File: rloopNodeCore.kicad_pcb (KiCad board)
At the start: 2 copper layers, 47 parts, among them P1 PWR_CONN_1X2, P2 CAN_IN_M12, P3 CAN_OUT_M12, U1 R-625.0P, U2 TYS01, U3 ISO1540, U4 MCP2562

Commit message: node core is almost done, awaiting review
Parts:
- removed the C4 at (172.7, 92.7)
- added C3: 100uF, Capacitors_SMD:c_elec_6.3x5.8, F.Cu at (153.0, 124.0)
- added C5: 100uF, Capacitors_SMD:c_elec_6.3x5.8, F.Cu at (163.0, 124.0)
- added C6: 10uF, Capacitors_SMD:C_1206_HandSoldering, F.Cu at (169.0, 124.0)
- added D2: D, Diodes_SMD:SMC_Standard, F.Cu at (144.0, 116.9)
- added F1: FUSE, -footprints:FUSEHOLDER-BLADE-LITTELFUSE-153, F.Cu at (136.4, 132.2)
- added F2: FUSE, -footprints:FUSEHOLDER-BLADE-LITTELFUSE-153, F.Cu at (144.0, 132.2)
- added P2: PWR_CONN_1X2, -footprints:CONN-TE-MICROMNL-2-PTH-MALE-RGT, F.Cu at (147.8, 143.6)
- A1: footprint -footprints:NODE-CORE -> -footprints:NODECORE
- A2: renamed from A3; footprint Pin_Headers:Pin_Header_Straight_2x20 -> -footprints:Raspberry-Pi-2-Model-B; moved to B.Cu
- C1: footprint Capacitors_SMD:C_2225 -> Capacitors_SMD:c_elec_6.3x5.8
- C2: value 10uF -> 100uF; footprint Capacitors_SMD:C_1210 -> Capacitors_SMD:c_elec_6.3x5.8
- moved A2 191.1 mm to (240.5, 140.0), turned to 90 degrees
- moved R2 165.3 mm to (232.0, 129.0), turned to 180 degrees
- moved A1 163.5 mm to (158.0, 42.0)
- moved R4 161.1 mm to (232.0, 124.0), turned to 180 degrees
- moved R10 156.9 mm to (230.0, 148.0), turned to 180 degrees
- moved A3 143.9 mm to (149.0, 55.0), turned to 0 degrees
- moved R9 141.9 mm to (231.8, 103.0), turned to 180 degrees
- moved R6 138.9 mm to (232.0, 96.0), turned to 180 degrees
- moved R7 135.5 mm to (232.0, 93.5), turned to 180 degrees
- moved D4 133.7 mm to (230.0, 150.0), turned to 180 degrees
- moved JP1 114.5 mm to (160.4, 96.0), turned to 180 degrees
- moved P1 109.1 mm to (132.6, 143.6), turned to 0 degrees
- moved R17 99.9 mm to (186.2, 106.5), turned to 90 degrees
- moved R1 99.2 mm to (165.0, 148.0), turned to 180 degrees
- moved U1 91.5 mm to (173.0, 149.0), turned to 90 degrees
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- renumbered A2 to A3, C8 to C10, C10 to C11, C6 to C12, C5 to C4, C3 to C7, C9 to C8, C7 to C9, D2 to D3, D3 to D4, D4 to D5, P2 to P3, P3 to P4, R2 to R10, R3 to R11, R6 to R12, R7 to R13, R8 to R14, R9 to R15, R10 to R16, R4 to R17, R5 to R18, R11 to R2, R12 to R3, R13 to R4, R15 to R5, R17 to R6, R18 to R7, R14 to R8, R16 to R9, U4 to U2, U2 to U4, W3 to W2, W2 to W3
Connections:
- A1 pad T29: (no net) -> SCL
- A1 pad T30: (no net) -> SDA
- A2 pad 39: Net-(A3-Pad39) -> GND
- A3 pad +3V3: (no net) -> +3V3
- A3 pad A10: (no net) -> A10
- A3 pad A11: (no net) -> A11
- A3 pad A12: (no net) -> A12
- A3 pad A13: (no net) -> A13
- A3 pad A14: (no net) -> A14
- A3 pad AGND: (no net) -> GNDA
- A3 pad AREF: (no net) -> AREF
- A3 pad GND1: (no net) -> GND
- A3 pad GND2: (no net) -> GND
- A3 pad GND3: (no net) -> GND
- A3 pad PROG: (no net) -> Net-(A3-PadPROG)
- A3 pad VBat: (no net) -> Net-(A3-PadVBat)
- A3 pad VIN: (no net) -> +5V
- A3 pad VUSB: (no net) -> Net-(A3-PadVUSB)
- C1 pad 1: +5V -> +24V
- C2 pad 1: +5V -> +24V
- JP1 pad 2: Net-(A2-Pad~) -> Net-(A3-PadPROG)
- P1 pad 2: Net-(D1-Pad2) -> Net-(F1-Pad1)
- P1 pad M1: Net-(P1-PadM1) -> GND
- P1 pad M2: Net-(P1-PadM2) -> GND
- P3 pad M1: Net-(P2-PadM1) -> GND
- P3 pad M2: Net-(P2-PadM2) -> GND
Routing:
- net +5V: track 0.00 -> 350.0 mm, vias 0 -> 9
- net +3V3: track 0.00 -> 285.1 mm, vias 0 -> 6
- net GND: track 0.00 -> 221.0 mm, vias 0 -> 38
- net TEENSY_CAN_TX: track 0.00 -> 105.0 mm, vias 0 -> 2
- net TEENSY_CAN_RX: track 0.00 -> 103.0 mm
- net 3V3_PI: track 0.00 -> 87.5 mm, vias 0 -> 3
- net PROG: track 0.00 -> 80.6 mm
- net ID1: track 0.00 -> 68.8 mm
- net ID2: track 0.00 -> 63.8 mm
- net Net-(A3-Pad19): track 0.00 -> 63.5 mm, vias 0 -> 2
- net Net-(A3-Pad18): track 0.00 -> 62.8 mm, vias 0 -> 1
- net ID3: track 0.00 -> 58.9 mm
- net AREF: track 0.00 -> 52.3 mm
- net SDA: track 0.00 -> 49.9 mm, vias 0 -> 2
- net PI_SDA: track 0.00 -> 47.9 mm
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- added copper zone on F.Cu, net +24V
- added copper zone on F.Cu, net +3V3
- added copper zone on F.Cu, net +5V
- added copper zone on B.Cu, net GND
- added copper zone on F.Cu, net GND
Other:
- board outline added: 170 x 110 mm
- net class +24V added: clearance 0.4, trace_width 0.25, via_dia 0.85, via_drill 0.5
- net class Default: trace_width 0.25 -> 0.2; via_dia 0.6 -> 0.85; via_drill 0.4 -> 0.5
- board text added: "+24V"
- board text added: "+3V3"
- board text added: "+5V"
- board text added: "Node Core rLoop V1 20160605"
- board text added: "PROG"

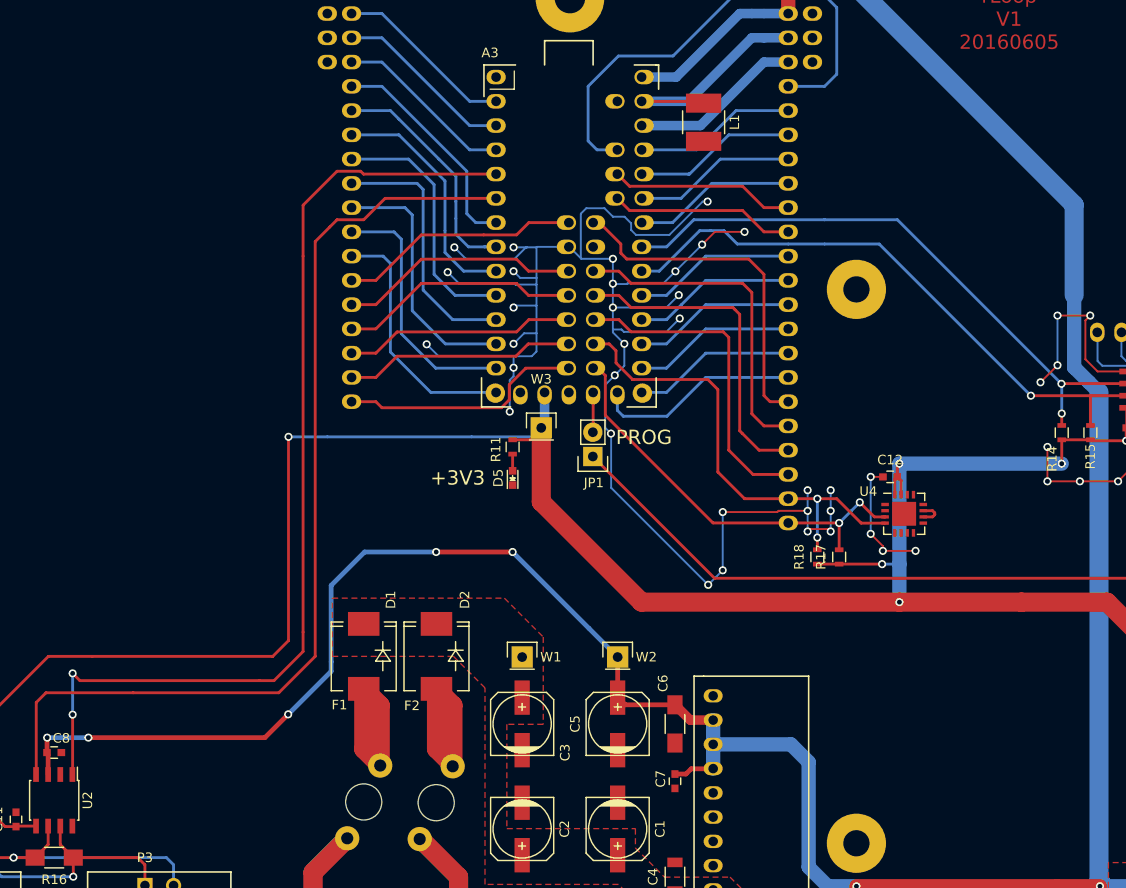
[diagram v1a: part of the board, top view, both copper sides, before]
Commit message: minor routing changes, some more vias
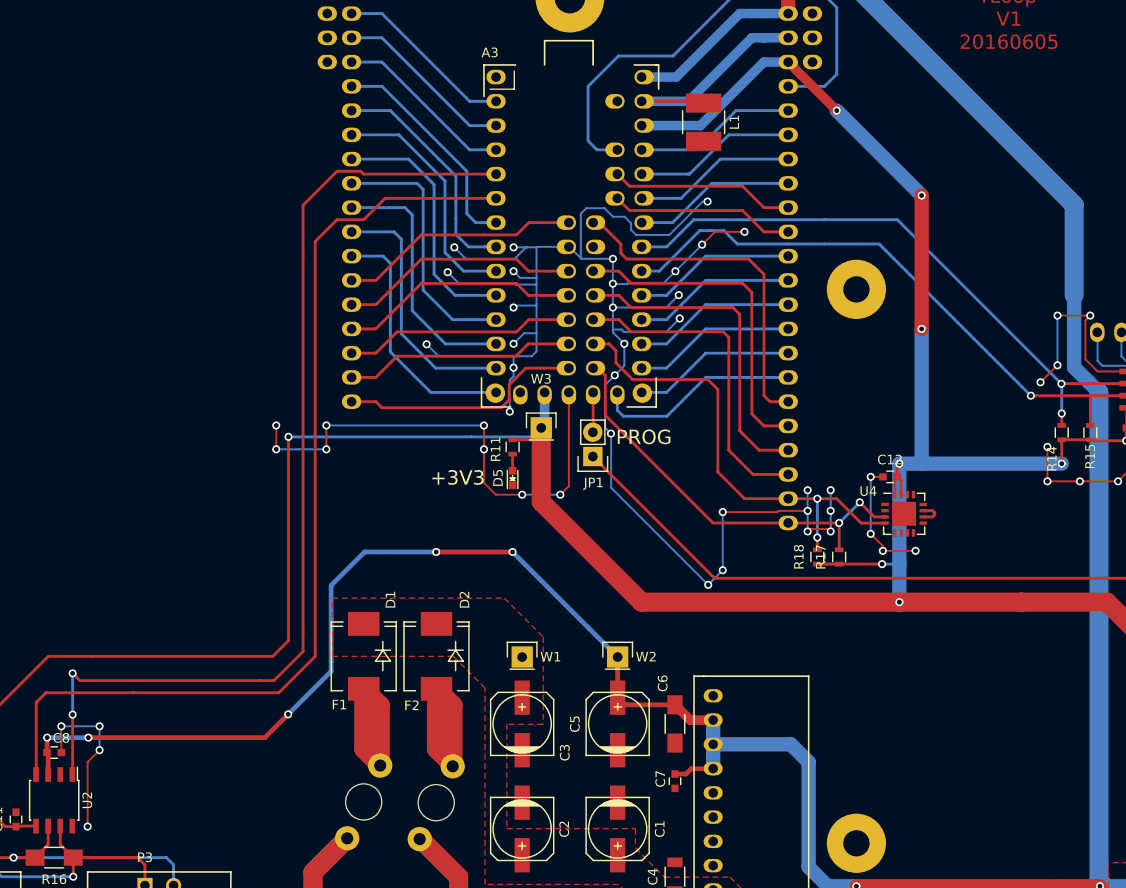
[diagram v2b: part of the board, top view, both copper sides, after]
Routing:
- net GND: track 221.0 -> 291.1 mm, vias 38 -> 50
- net +3V3: track 285.1 -> 332.9 mm, vias 6 -> 9
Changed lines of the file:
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@@
   (general
     (links 215)
-    (no_connects 1)
-    (area 72.924999 41.924999 243.075001 152.075001)
+    (no_connects 0)
+    (area 72.514999 40.175 243.485001 168.985001)
     (thickness 1.6)
     (drawings 13)
-    (tracks 835)
+    (tracks 872)
     (zones 0)
     (modules 53)
@@
   )
   (setup
-    (last_trace_width 0.2)
+    (last_trace_width 1.5)
     (user_trace_width 0.203)
     (user_trace_width 0.3)
@@
     (aux_axis_origin 0 0)
     (grid_origin 158 42)
-    (visible_elements 7FFFFFFF)
+    (visible_elements 7FFEF7FF)
     (pcbplotparams
       (layerselection 0x00030_80000001)
@@
   (segment (start 171.289 63.89) (end 175.399 59.78) (width 0.3) (layer B.Cu) (net 28))
   (segment (start 175.399 59.78) (end 180.86 59.78) (width 0.3) (layer B.Cu) (net 28))
+  (segment (start 194.83 82.64) (end 194.83 96.61) (width 1.5) (layer B.Cu) (net 29))
+  (via (at 194.83 68.67) (size 0.85) (drill 0.5) (layers F.Cu B.Cu) (net 29))
+  (segment (start 194.83 68.67) (end 194.83 82.64) (width 1.5) (layer F.Cu) (net 29))
+  (via (at 194.83 82.64) (size 0.85) (drill 0.5) (layers F.Cu B.Cu) (net 29))
+  (segment (start 180.86 54.7) (end 185.94 59.78) (width 1) (layer F.Cu) (net 29))
+  (via (at 185.94 59.78) (size 0.85) (drill 0.5) (layers F.Cu B.Cu) (net 29))
+  (segment (start 185.94 59.78) (end 194.83 68.67) (width 1.5) (layer B.Cu) (net 29))
+  (segment (start 194.83 96.61) (end 194.83 96.75) (width 1.5) (layer B.Cu) (net 29))
   (segment (start 152 94.25) (end 153.85 94.25) (width 0.3) (layer F.Cu) (net 29))
   (segment (start 153.85 94.25) (end 155 93.1) (width 0.3) (layer F.Cu) (net 29))
@@
   (segment (start 209.4 94.2) (end 209.5 94.25) (width 0.3) (layer F.Cu) (net 29))
   (segment (start 209.5 94.25) (end 209.5 96.7) (width 0.3) (layer F.Cu) (net 29))
+  (via (at 209.5 96.75) (size 0.85) (drill 0.5) (layers F.Cu B.Cu) (net 29))
+  (segment (start 209.6 96.8) (end 209.5 96.75) (width 0.3) (layer F.Cu) (net 29))
   (segment (start 209.5 96.7) (end 209.6 96.8) (width 0.3) (layer F.Cu) (net 29))
-  (segment (start 209.6 96.8) (end 209.5 96.75) (width 0.3) (layer F.Cu) (net 29))
-  (segment (start 192.5 96.75) (end 209.5 96.75) (width 1.5) (layer B.Cu) (net 29))
-  (via (at 209.5 96.75) (size 0.85) (drill 0.5) (layers F.Cu B.Cu) (net 29))
+  (segment (start 192.5 96.75) (end 194.83 96.75) (width 1.5) (layer B.Cu) (net 29))
+  (segment (start 194.83 96.75) (end 209.5 96.75) (width 1.5) (layer B.Cu) (net 29))
   (segment (start 192.278 98.134) (end 192.278 96.972) (width 0.3) (layer F.Cu) (net 29))
   (segment (start 192.278 96.972) (end 192.5 96.75) (width 0.3) (layer F.Cu) (net 29))
@@
   (segment (start 238.27 129.09) (end 238.27 131.67) (width 1) (layer F.Cu) (net 31))
   (segment (start 238.27 131.67) (end 238.27 131.63) (width 1) (layer F.Cu) (net 31))
+  (segment (start 108.75 124.25) (end 108.75 126.75) (width 0.2) (layer B.Cu) (net 32))
+  (via (at 104.75 124.25) (size 0.85) (drill 0.5) (layers F.Cu B.Cu) (net 32))
+  (segment (start 104.75 124.25) (end 108.75 124.25) (width 0.2) (layer B.Cu) (net 32))
+  (via (at 108.75 124.25) (size 0.85) (drill 0.5) (layers F.Cu B.Cu) (net 32))
+  (segment (start 104.75 127) (end 104.75 124.25) (width 0.2) (layer F.Cu) (net 32))
+  (via (at 107.5 134.75) (size 0.85) (drill 0.5) (layers F.Cu B.Cu) (net 32))
+  (segment (start 107.5 128) (end 107.5 134.75) (width 0.2) (layer F.Cu) (net 32))
+  (segment (start 108.75 126.75) (end 107.5 128) (width 0.2) (layer F.Cu) (net 32))
+  (via (at 108.75 126.75) (size 0.85) (drill 0.5) (layers F.Cu B.Cu) (net 32))
+  (segment (start 149 95.25) (end 149 92.75) (width 0.2) (layer F.Cu) (net 32))
+  (segment (start 150.25 100) (end 149 98.75) (width 0.2) (layer F.Cu) (net 32))
+  (segment (start 149 98.75) (end 149 95.25) (width 0.2) (layer F.Cu) (net 32))
+  (via (at 149 95.25) (size 0.85) (drill 0.5) (layers F.Cu B.Cu) (net 32))
+  (segment (start 157.89 89.29) (end 157.89 99.11) (width 0.2) (layer F.Cu) (net 32))
+  (via (at 153 100) (size 0.85) (drill 0.5) (layers F.Cu B.Cu) (net 32))
+  (segment (start 157 100) (end 153 100) (width 0.2) (layer B.Cu) (net 32))
+  (via (at 157 100) (size 0.85) (drill 0.5) (layers F.Cu B.Cu) (net 32))
+  (segment (start 157.89 99.11) (end 157 100) (width 0.2) (layer F.Cu) (net 32))
+  (segment (start 153 100) (end 150.25 100) (width 0.2) (layer F.Cu) (net 32))
+  (via (at 127.25 92.75) (size 0.85) (drill 0.5) (layers F.Cu B.Cu) (net 32))
+  (segment (start 127.25 95.25) (end 127.25 92.75) (width 0.2) (layer F.Cu) (net 32))
+  (via (at 127.25 95.25) (size 0.85) (drill 0.5) (layers F.Cu B.Cu) (net 32))
+  (segment (start 132.5 95.25) (end 127.25 95.25) (width 0.2) (layer B.Cu) (net 32))
+  (via (at 132.5 95.25) (size 0.85) (drill 0.5) (layers F.Cu B.Cu) (net 32))
+  (segment (start 132.5 92.75) (end 132.5 95.25) (width 0.2) (layer F.Cu) (net 32))
+  (via (at 132.5 92.75) (size 0.85) (drill 0.5) (layers F.Cu B.Cu) (net 32))
+  (segment (start 149 92.75) (end 132.5 92.75) (width 0.2) (layer B.Cu) (net 32))
+  (via (at 149 92.75) (size 0.85) (drill 0.5) (layers F.Cu B.Cu) (net 32))
   (segment (start 209.054 81.243) (end 209.054 86.45) (width 0.2) (layer B.Cu) (net 32))
   (via (at 209.054 86.45) (size 0.85) (drill 0.5) (layers F.Cu B.Cu) (net 32))

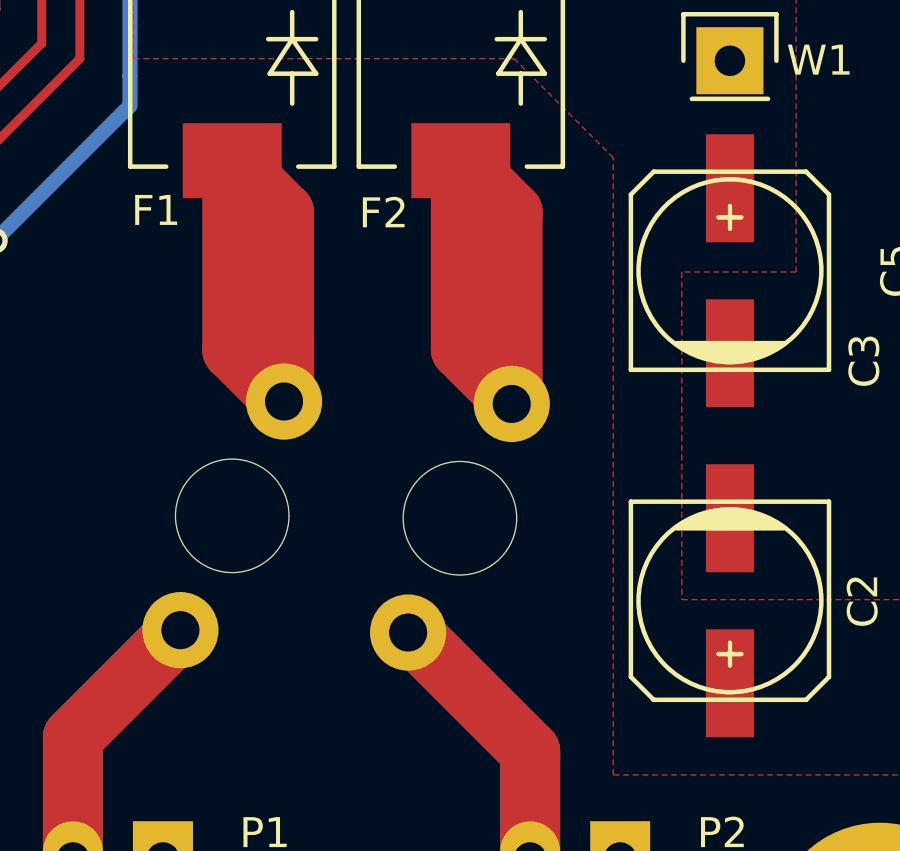
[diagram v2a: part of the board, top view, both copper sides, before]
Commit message: F2 was offset by a single hair
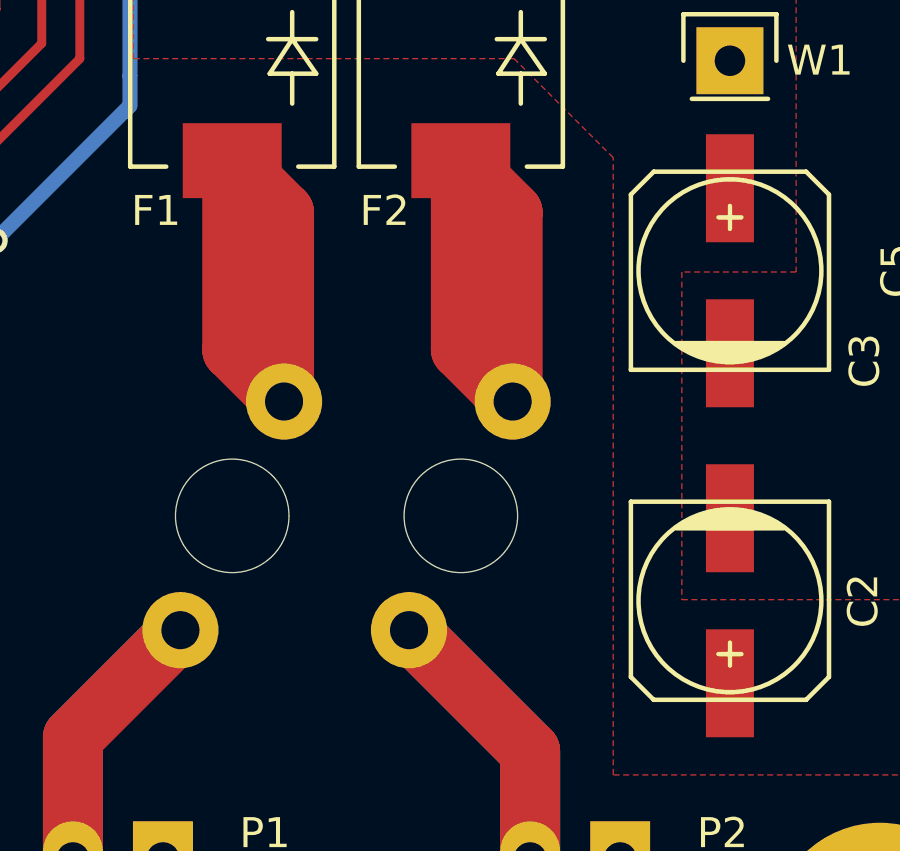
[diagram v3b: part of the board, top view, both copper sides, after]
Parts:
- moved F2 0.09 mm to (144.0, 132.2)
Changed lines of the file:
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@@
   )
   (setup
-    (last_trace_width 1.5)
+    (last_trace_width 0.2)
     (user_trace_width 0.203)
     (user_trace_width 0.3)
@@
   )
   (module -footprints:FUSEHOLDER-BLADE-LITTELFUSE-153 (layer F.Cu)
-    (at 144 132.25 180)
+    (at 144.03 132.17 180)
     (fp_text reference F2 (at 2.54 10.16 180) (layer F.SilkS)
       (effects (font (size 1 1) (thickness 0.15)))
